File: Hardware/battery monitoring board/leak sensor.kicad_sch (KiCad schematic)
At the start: 11 parts, among them J2 Conn_01x02, J3 Conn_01x02, J4 Conn_01x02, J5 Conn_01x02, Q1 PNP

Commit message: updated battery board pt.II
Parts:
- TP1: footprint Library:Test Pads -> PCM_4ms_TestPoint:TestPoint_Pad_06
- renumbered D4 to D6
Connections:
- net +3V3: now also Q1.3 (E); no longer Q1.2 (E)
- net LEAK_SIGNAL: now also Q1.1 (C); no longer Q1.3 (C)
- net at R7.2, R8.2: now also Q1.2 (B); no longer Q1.1 (B)
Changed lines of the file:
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@@
   (symbol (lib_id "power:+3V3") (at 105.41 46.99 0) (unit 1)
     (in_bom yes) (on_board yes) (dnp no) (fields_autoplaced)
-    (property "Reference" "#PWR021" (at 105.41 50.8 0)
+    (property "Reference" "#PWR027" (at 105.41 50.8 0)
       (effects (font (size 1.27 1.27)) hide)
     )
@@
       (project "battery monitoring board"
         (path "/bf623d80-ca5a-491f-9daa-4dffbeba5279/7fa71be0-4e2c-431c-85f4-b0f15423b53d"
-          (reference "#PWR021") (unit 1)
+          (reference "#PWR027") (unit 1)
         )
       )
@@
       (project "battery monitoring board"
         (path "/bf623d80-ca5a-491f-9daa-4dffbeba5279/7fa71be0-4e2c-431c-85f4-b0f15423b53d"
-          (reference "#PWR022") (unit 1)
+          (reference "#PWR028") (unit 1)
         )
       )
@@
       (effects (font (size 1.27 1.27)) (justify left))
     )
-    (property "Footprint" "Library:Test Pads" (at 120.65 62.23 0)
+    (property "Footprint" "PCM_4ms_TestPoint:TestPoint_Pad_06" (at 120.65 62.23 0)
       (effects (font (size 1.27 1.27)) hide)
     )
@@
         )
         (path "/bf623d80-ca5a-491f-9daa-4dffbeba5279/7fa71be0-4e2c-431c-85f4-b0f15423b53d"
-          (reference "TP11") (unit 1)
+          (reference "TP12") (unit 1)
         )
       )
@@
       (project "battery monitoring board"
         (path "/bf623d80-ca5a-491f-9daa-4dffbeba5279/7fa71be0-4e2c-431c-85f4-b0f15423b53d"
-          (reference "#PWR020") (unit 1)
+          (reference "#PWR026") (unit 1)
         )
       )
@@
       (project "battery monitoring board"
         (path "/bf623d80-ca5a-491f-9daa-4dffbeba5279/7fa71be0-4e2c-431c-85f4-b0f15423b53d"
-          (reference "R12") (unit 1)
+          (reference "R14") (unit 1)
         )
       )
@@
       (project "battery monitoring board"
         (path "/bf623d80-ca5a-491f-9daa-4dffbeba5279/7fa71be0-4e2c-431c-85f4-b0f15423b53d"
-          (reference "R13") (unit 1)
+          (reference "R15") (unit 1)
         )
       )
@@
       (project "battery monitoring board"
         (path "/bf623d80-ca5a-491f-9daa-4dffbeba5279/7fa71be0-4e2c-431c-85f4-b0f15423b53d"
-          (reference "R14") (unit 1)
+          (reference "R16") (unit 1)
         )
       )
@@
   (symbol (lib_id "Device:LED") (at 115.57 80.01 90) (unit 1)
     (in_bom yes) (on_board yes) (dnp no) (fields_autoplaced)
-    (property "Reference" "D4" (at 119.38 80.3275 90)
+    (property "Reference" "D6" (at 119.38 80.3275 90)
       (effects (font (size 1.27 1.27)) (justify right))
     )
@@
       (project "battery monitoring board"
         (path "/bf623d80-ca5a-491f-9daa-4dffbeba5279/7fa71be0-4e2c-431c-85f4-b0f15423b53d"
-          (reference "D4") (unit 1)
+          (reference "D6") (unit 1)
         )
       )
@@
       (project "battery monitoring board"
         (path "/bf623d80-ca5a-491f-9daa-4dffbeba5279/7fa71be0-4e2c-431c-85f4-b0f15423b53d"
-          (reference "R11") (unit 1)
+          (reference "R13") (unit 1)
         )
       )
@@
       (effects (font (size 1.27 1.27)) hide)
     )
-    (property "Sim.Pins" "1=B 2=E 3=C" (at 95.25 48.26 0)
-      (effects (font (size 1.27 1.27)) hide)
-    )
+    (property "Sim.Pins" "1=C 2=B 3=E" (at 95.25 48.26 0)
+      (effects (font (size 1.27 1.27)) hide)
+    )

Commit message: finalized battery board !!
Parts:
- renumbered D6 to D5
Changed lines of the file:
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@@
   (symbol (lib_id "power:+3V3") (at 105.41 46.99 0) (unit 1)
     (in_bom yes) (on_board yes) (dnp no) (fields_autoplaced)
-    (property "Reference" "#PWR027" (at 105.41 50.8 0)
+    (property "Reference" "#PWR028" (at 105.41 50.8 0)
       (effects (font (size 1.27 1.27)) hide)
     )
@@
       (project "battery monitoring board"
         (path "/bf623d80-ca5a-491f-9daa-4dffbeba5279/7fa71be0-4e2c-431c-85f4-b0f15423b53d"
-          (reference "#PWR027") (unit 1)
+          (reference "#PWR028") (unit 1)
         )
       )
@@
       (project "battery monitoring board"
         (path "/bf623d80-ca5a-491f-9daa-4dffbeba5279/7fa71be0-4e2c-431c-85f4-b0f15423b53d"
-          (reference "#PWR028") (unit 1)
+          (reference "#PWR029") (unit 1)
         )
       )
@@
       (project "battery monitoring board"
         (path "/bf623d80-ca5a-491f-9daa-4dffbeba5279/7fa71be0-4e2c-431c-85f4-b0f15423b53d"
-          (reference "#PWR026") (unit 1)
+          (reference "#PWR027") (unit 1)
         )
       )
@@
       (project "battery monitoring board"
         (path "/bf623d80-ca5a-491f-9daa-4dffbeba5279/7fa71be0-4e2c-431c-85f4-b0f15423b53d"
+          (reference "R13") (unit 1)
+        )
+      )
+    )
+  )
+  (symbol (lib_id "Device:R_US") (at 105.41 69.85 0) (unit 1)
+    (in_bom yes) (on_board yes) (dnp no)
+    (property "Reference" "R9" (at 107.95 71.12 90)
+      (effects (font (size 1.27 1.27)) (justify left))
+    )
+    (property "Value" "1k" (at 102.87 71.12 90)
+      (effects (font (size 1.27 1.27)) (justify left))
+    )
+    (property "Footprint" "Resistor_SMD:R_0805_2012Metric_Pad1.20x1.40mm_HandSolder" (at 106.426 70.104 90)
+      (effects (font (size 1.27 1.27)) hide)
+    )
+    (property "Datasheet" "~" (at 105.41 69.85 0)
+      (effects (font (size 1.27 1.27)) hide)
+    )
+    (pin "1")
+    (pin "2")
+    (instances
+      (project "leak sensor"
+        (path "/127822e7-fd70-4fb4-952a-2fa8fdde2438"
+          (reference "R9") (unit 1)
+        )
+      )
+      (project "battery monitoring board"
+        (path "/bf623d80-ca5a-491f-9daa-4dffbeba5279/7fa71be0-4e2c-431c-85f4-b0f15423b53d"
           (reference "R14") (unit 1)
         )
@@
     )
   )
-  (symbol (lib_id "Device:R_US") (at 105.41 69.85 0) (unit 1)
-    (in_bom yes) (on_board yes) (dnp no)
-    (property "Reference" "R9" (at 107.95 71.12 90)
-      (effects (font (size 1.27 1.27)) (justify left))
-    )
-    (property "Value" "1k" (at 102.87 71.12 90)
-      (effects (font (size 1.27 1.27)) (justify left))
-    )
-    (property "Footprint" "Resistor_SMD:R_0805_2012Metric_Pad1.20x1.40mm_HandSolder" (at 106.426 70.104 90)
-      (effects (font (size 1.27 1.27)) hide)
-    )
-    (property "Datasheet" "~" (at 105.41 69.85 0)
-      (effects (font (size 1.27 1.27)) hide)
-    )
-    (pin "1")
-    (pin "2")
-    (instances
-      (project "leak sensor"
-        (path "/127822e7-fd70-4fb4-952a-2fa8fdde2438"
-          (reference "R9") (unit 1)
+  (symbol (lib_id "Device:R_US") (at 115.57 69.85 0) (unit 1)
+    (in_bom yes) (on_board yes) (dnp no)
+    (property "Reference" "R10" (at 118.11 71.12 90)
+      (effects (font (size 1.27 1.27)) (justify left))
+    )
+    (property "Value" "100" (at 113.03 71.12 90)
+      (effects (font (size 1.27 1.27)) (justify left))
+    )
+    (property "Footprint" "Resistor_SMD:R_0805_2012Metric_Pad1.20x1.40mm_HandSolder" (at 116.586 70.104 90)
+      (effects (font (size 1.27 1.27)) hide)
+    )
+    (property "Datasheet" "~" (at 115.57 69.85 0)
+      (effects (font (size 1.27 1.27)) hide)
+    )
+    (pin "1")
+    (pin "2")
+    (instances
+      (project "leak sensor"
+        (path "/127822e7-fd70-4fb4-952a-2fa8fdde2438"
+          (reference "R10") (unit 1)
         )
       )
@@
         (path "/bf623d80-ca5a-491f-9daa-4dffbeba5279/7fa71be0-4e2c-431c-85f4-b0f15423b53d"
           (reference "R15") (unit 1)
-        )
-      )
-    )
-  )
-  (symbol (lib_id "Device:R_US") (at 115.57 69.85 0) (unit 1)
-    (in_bom yes) (on_board yes) (dnp no)
-    (property "Reference" "R10" (at 118.11 71.12 90)
-      (effects (font (size 1.27 1.27)) (justify left))
-    )
-    (property "Value" "100" (at 113.03 71.12 90)
-      (effects (font (size 1.27 1.27)) (justify left))
-    )
-    (property "Footprint" "Resistor_SMD:R_0805_2012Metric_Pad1.20x1.40mm_HandSolder" (at 116.586 70.104 90)
-      (effects (font (size 1.27 1.27)) hide)
-    )
-    (property "Datasheet" "~" (at 115.57 69.85 0)
-      (effects (font (size 1.27 1.27)) hide)
-    )
-    (pin "1")
-    (pin "2")
-    (instances
-      (project "leak sensor"
-        (path "/127822e7-fd70-4fb4-952a-2fa8fdde2438"
-          (reference "R10") (unit 1)
-        )
-      )
-      (project "battery monitoring board"
-        (path "/bf623d80-ca5a-491f-9daa-4dffbeba5279/7fa71be0-4e2c-431c-85f4-b0f15423b53d"
-          (reference "R16") (unit 1)
         )
       )
@@
   (symbol (lib_id "Device:LED") (at 115.57 80.01 90) (unit 1)
     (in_bom yes) (on_board yes) (dnp no) (fields_autoplaced)
-    (property "Reference" "D6" (at 119.38 80.3275 90)
+    (property "Reference" "D5" (at 119.38 80.3275 90)
       (effects (font (size 1.27 1.27)) (justify right))
     )
@@
       (project "battery monitoring board"
         (path "/bf623d80-ca5a-491f-9daa-4dffbeba5279/7fa71be0-4e2c-431c-85f4-b0f15423b53d"
-          (reference "D6") (unit 1)
+          (reference "D5") (unit 1)
         )
       )
@@
       (project "battery monitoring board"
         (path "/bf623d80-ca5a-491f-9daa-4dffbeba5279/7fa71be0-4e2c-431c-85f4-b0f15423b53d"
-          (reference "R13") (unit 1)
-        )
-      )
+          (reference "R12") (unit 1)
+        )
+      )

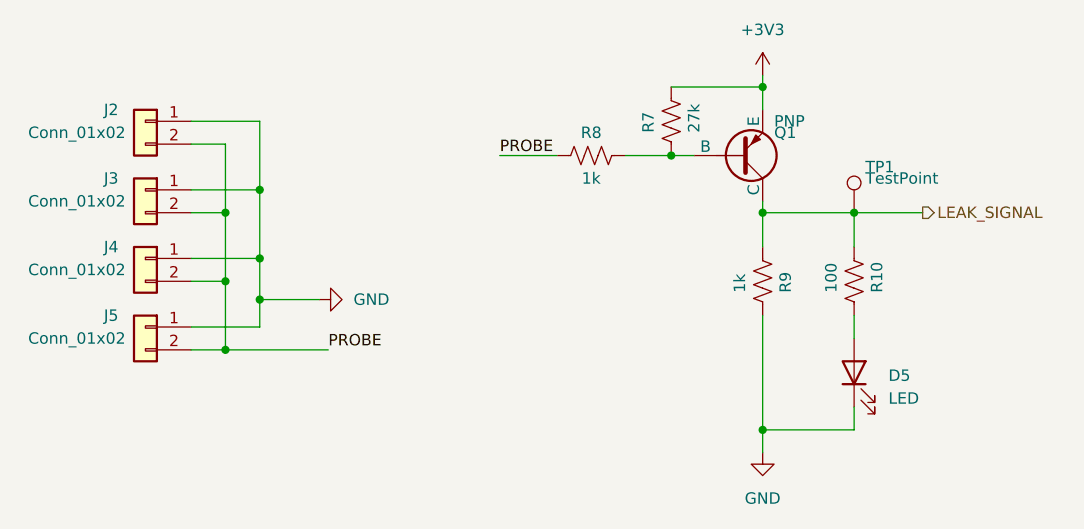
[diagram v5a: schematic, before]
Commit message: resolved erc/drc issues
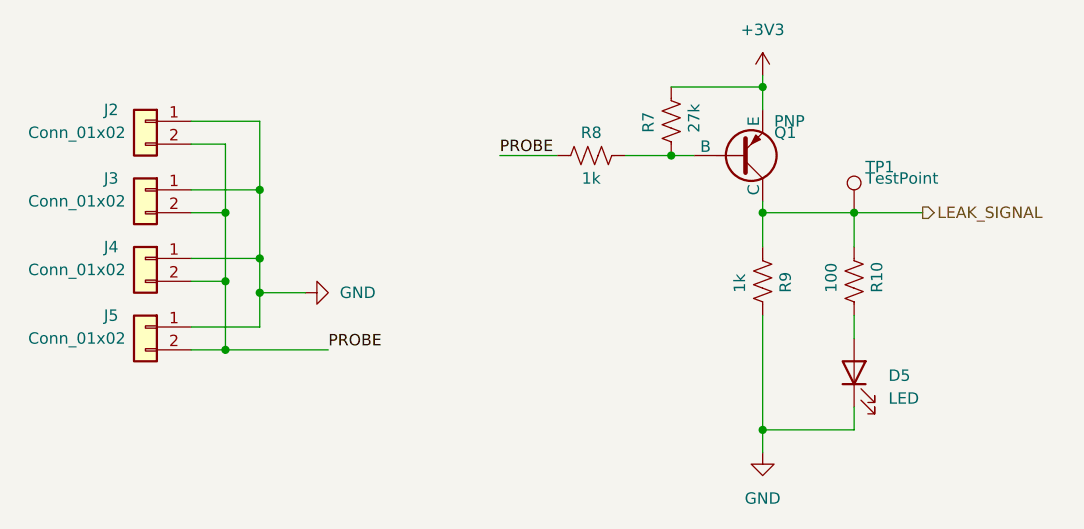
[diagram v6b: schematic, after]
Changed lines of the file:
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@@
   (junction (at 105.41 86.36) (diameter 0) (color 0 0 0 0)
   )
+  (junction (at 49.53 71.12) (diameter 0) (color 0 0 0 0)
+  )
   (junction (at 115.57 62.23) (diameter 0) (color 0 0 0 0)
   )
-  (junction (at 49.53 71.882) (diameter 0) (color 0 0 0 0)
-  )
   (wire (pts (xy 41.91 54.61) (xy 45.72 54.61))
     (stroke (width 0) (type default))
@@
     (stroke (width 0) (type default))
   )
-  (wire (pts (xy 49.53 71.882) (xy 49.53 74.93))
-    (stroke (width 0) (type default))
-  )
   (wire (pts (xy 115.57 73.66) (xy 115.57 76.2))
     (stroke (width 0) (type default))
@@
     (stroke (width 0) (type default))
   )
-  (wire (pts (xy 49.53 67.31) (xy 49.53 71.882))
+  (wire (pts (xy 49.53 67.31) (xy 49.53 71.12))
     (stroke (width 0) (type default))
   )
@@
     (stroke (width 0) (type default))
   )
+  (wire (pts (xy 49.53 71.12) (xy 54.61 71.12))
+    (stroke (width 0) (type default))
+  )
   (wire (pts (xy 41.91 52.07) (xy 49.53 52.07))
     (stroke (width 0) (type default))
@@
     (stroke (width 0) (type default))
   )
-  (wire (pts (xy 49.53 71.882) (xy 56.134 71.882))
+  (wire (pts (xy 49.53 71.12) (xy 49.53 74.93))
     (stroke (width 0) (type default))
   )
@@
       (project "battery monitoring board"
         (path "/bf623d80-ca5a-491f-9daa-4dffbeba5279/7fa71be0-4e2c-431c-85f4-b0f15423b53d"
-          (reference "- J6 +1") (unit 1)
+          (reference "J6") (unit 1)
         )
       )
@@
       (project "battery monitoring board"
         (path "/bf623d80-ca5a-491f-9daa-4dffbeba5279/7fa71be0-4e2c-431c-85f4-b0f15423b53d"
-          (reference "- J8 +1") (unit 1)
+          (reference "J8") (unit 1)
         )
       )
@@
     )
   )
-  (symbol (lib_id "power:GND") (at 56.134 71.882 90) (unit 1)
+  (symbol (lib_id "power:GND") (at 54.61 71.12 90) (unit 1)
     (in_bom yes) (on_board yes) (dnp no) (fields_autoplaced)
-    (property "Reference" "#PWR05" (at 62.484 71.882 0)
-      (effects (font (size 1.27 1.27)) hide)
-    )
-    (property "Value" "GND" (at 59.944 71.882 90)
+    (property "Reference" "#PWR05" (at 60.96 71.12 0)
+      (effects (font (size 1.27 1.27)) hide)
+    )
+    (property "Value" "GND" (at 58.42 71.12 90)
       (effects (font (size 1.27 1.27)) (justify right))
     )
-    (property "Footprint" "" (at 56.134 71.882 0)
-      (effects (font (size 1.27 1.27)) hide)
-    )
-    (property "Datasheet" "" (at 56.134 71.882 0)
+    (property "Footprint" "" (at 54.61 71.12 0)
+      (effects (font (size 1.27 1.27)) hide)
+    )
+    (property "Datasheet" "" (at 54.61 71.12 0)
       (effects (font (size 1.27 1.27)) hide)
     )
@@
       (project "battery monitoring board"
         (path "/bf623d80-ca5a-491f-9daa-4dffbeba5279/7fa71be0-4e2c-431c-85f4-b0f15423b53d"
-          (reference "- J7 +1") (unit 1)
+          (reference "J7") (unit 1)
         )
       )
@@
       (project "battery monitoring board"
         (path "/bf623d80-ca5a-491f-9daa-4dffbeba5279/7fa71be0-4e2c-431c-85f4-b0f15423b53d"
-          (reference " - J5 +1") (unit 1)
-        )
-      )
+          (reference "J5") (unit 1)
+        )
+      )
